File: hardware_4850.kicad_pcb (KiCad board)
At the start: 4 copper layers, 104 x 79 mm, 250 parts, among them J1 +, J10 Enable, J11 CAN_IN, J12 CAN_OUT, J13 Debug, J2 Display, J3 A, J4 HALL, J5 B, J6 MOT_AUX, J7 C, J8 GND, J9 CRANK, P1 SWD, Q1 IPT015N10N5, Q2 IPT015N10N5, Q3 IPT015N10N5, Q4 IPT015N10N5, Q5 IPT015N10N5, Q6 IPT015N10N5, U1 1EDN7550B, U10 LM5008, U11 XC6206P332MR, U12 XC6206P332MR, U13 LMR12010X, U14 STM32G473VCTx, U15 SN65HVD230, U2 INA240A2PWR, U3 1EDN7550B, U4 1EDN7550B, U5 INA240A2PWR, U6 1EDN7550B, U7 1EDN7550B, U8 INA240A2PWR, U9 1EDN7550B, Y1 8MHz

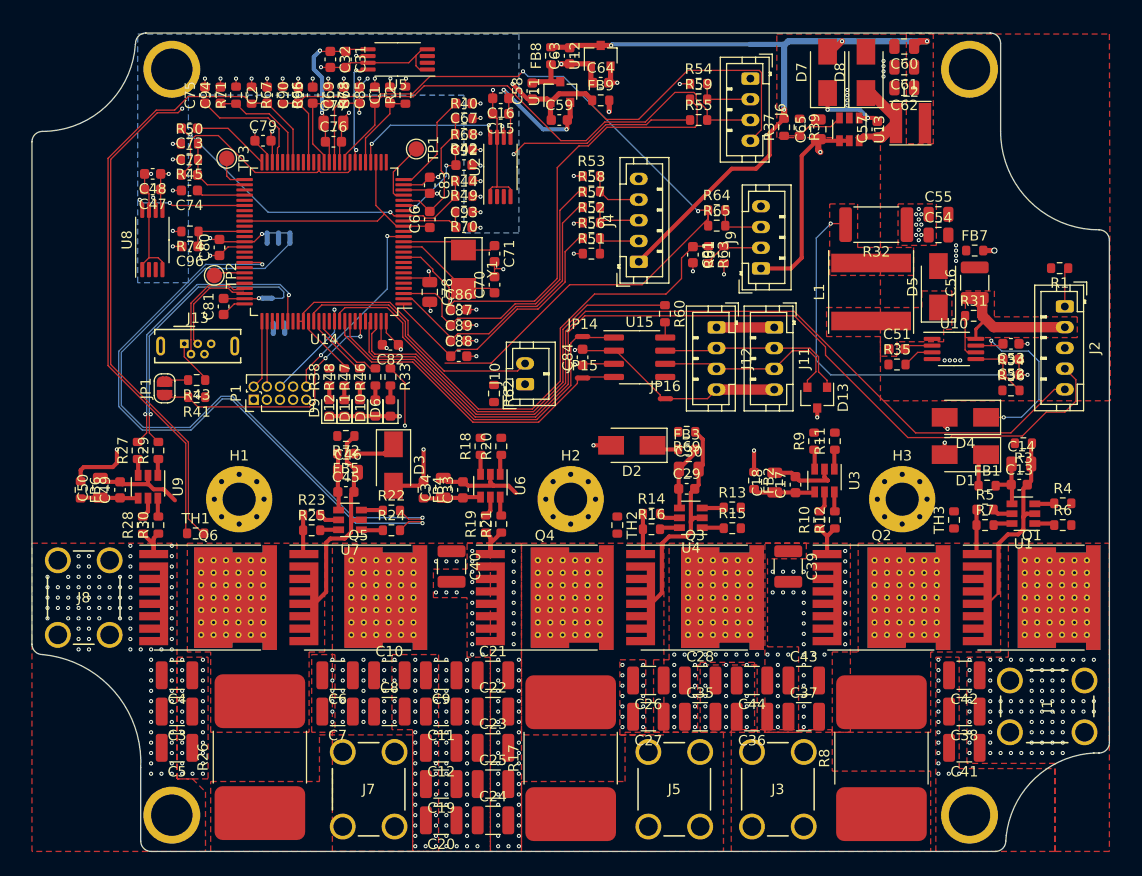
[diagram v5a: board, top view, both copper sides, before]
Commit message: added some more caps for decouppling
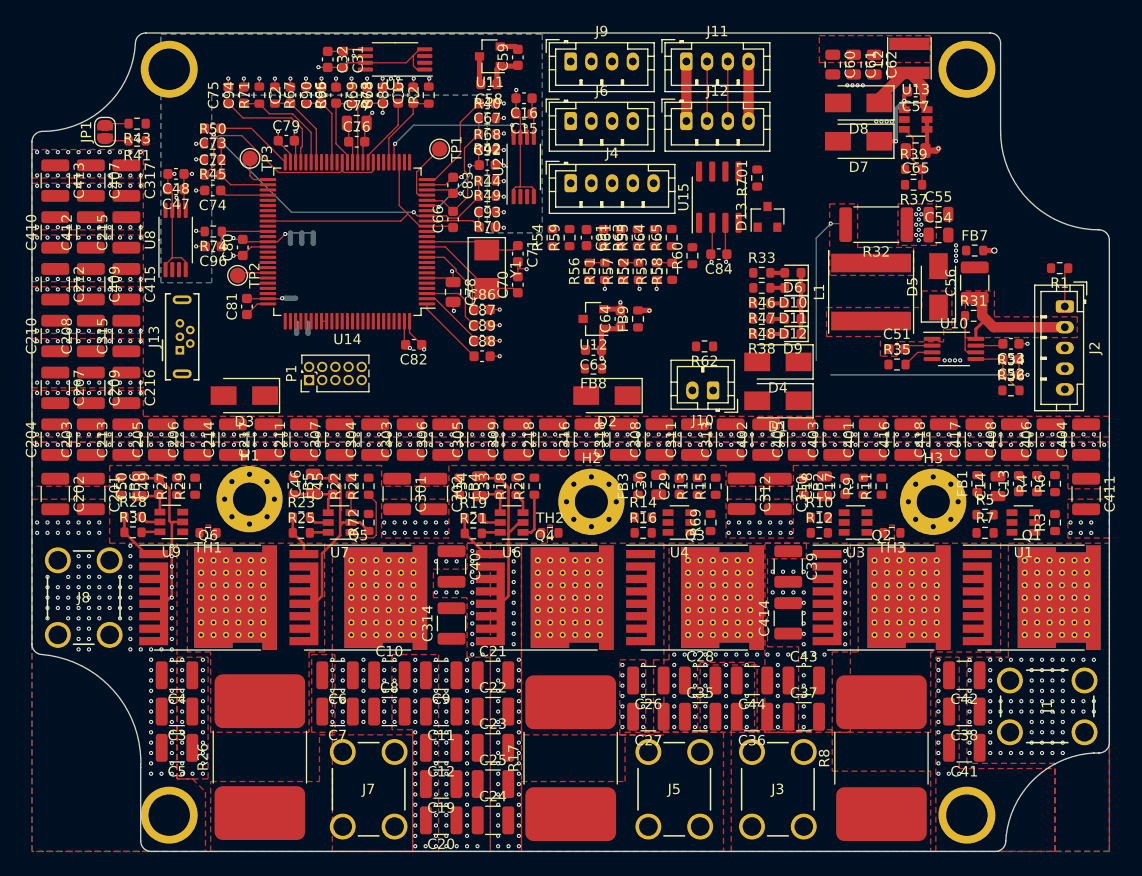
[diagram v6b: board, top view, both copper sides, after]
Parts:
- removed JP14: CAN_TX, NetTie:NetTie-2_SMD_Pad0.5mm
- removed JP15: CAN_RX, NetTie:NetTie-2_SMD_Pad0.5mm
- removed JP16: CAN_GND, NetTie:NetTie-2_SMD_Pad0.5mm
- added C201: 4u7, Capacitor_SMD:C_1210_3225Metric, F.Cu at (83.2, 94.0)
- added C202: 4u7, Capacitor_SMD:C_1210_3225Metric, F.Cu at (79.8, 94.0)
- added C203: 4u7, Capacitor_SMD:C_1210_3225Metric, F.Cu at (83.2, 88.8)
- added C204: 4u7, Capacitor_SMD:C_1210_3225Metric, F.Cu at (79.8, 88.8)
- added C205: 4u7, Capacitor_SMD:C_1210_3225Metric, F.Cu at (90.0, 88.8)
- added C206: 4u7, Capacitor_SMD:C_1210_3225Metric, F.Cu at (93.5, 88.8)
- added C207: 4u7, Capacitor_SMD:C_1210_3225Metric, F.Cu at (79.8, 83.8)
- added C208: 4u7, Capacitor_SMD:C_1210_3225Metric, F.Cu at (83.2, 78.8)
- added C209: 4u7, Capacitor_SMD:C_1210_3225Metric, F.Cu at (83.2, 83.8)
- added C210: 4u7, Capacitor_SMD:C_1210_3225Metric, F.Cu at (79.8, 78.8)
- added C211: 4u7, Capacitor_SMD:C_1210_3225Metric, F.Cu at (103.8, 88.8)
- added C212: 4u7, Capacitor_SMD:C_1210_3225Metric, F.Cu at (79.8, 73.8)
- added C213: 4u7, Capacitor_SMD:C_1210_3225Metric, F.Cu at (86.6, 88.8)
- added C214: 4u7, Capacitor_SMD:C_1210_3225Metric, F.Cu at (96.9, 88.8)
- added C215: 4u7, Capacitor_SMD:C_1210_3225Metric, F.Cu at (86.6, 68.8)
- added C216: 4u7, Capacitor_SMD:C_1210_3225Metric, F.Cu at (86.6, 83.8)
- added C217: 4u7, Capacitor_SMD:C_1210_3225Metric, F.Cu at (100.3, 88.8)
- added C218: 4u7, Capacitor_SMD:C_1210_3225Metric, F.Cu at (127.8, 88.8)
- added C301: 4u7, Capacitor_SMD:C_1210_3225Metric, F.Cu at (112.8, 94.0)
- added C302: 4u7, Capacitor_SMD:C_1210_3225Metric, F.Cu at (116.2, 94.0)
- added C303: 4u7, Capacitor_SMD:C_1210_3225Metric, F.Cu at (114.1, 88.8)
- added C304: 4u7, Capacitor_SMD:C_1210_3225Metric, F.Cu at (110.6, 88.8)
- added C305: 4u7, Capacitor_SMD:C_1210_3225Metric, F.Cu at (120.9, 88.8)
- added C306: 4u7, Capacitor_SMD:C_1210_3225Metric, F.Cu at (117.5, 88.8)
- added C307: 4u7, Capacitor_SMD:C_1210_3225Metric, F.Cu at (107.2, 88.8)
- added C308: 4u7, Capacitor_SMD:C_1210_3225Metric, F.Cu at (138.1, 88.8)
- added C309: 4u7, Capacitor_SMD:C_1210_3225Metric, F.Cu at (124.4, 88.8)
- added C310: 4u7, Capacitor_SMD:C_1210_3225Metric, F.Cu at (149.5, 94.0)
- added C311: 4u7, Capacitor_SMD:C_1210_3225Metric, F.Cu at (141.5, 88.8)
- added C312: 4u7, Capacitor_SMD:C_1210_3225Metric, F.Cu at (146.0, 94.0)
- added C313: 4u7, Capacitor_SMD:C_1210_3225Metric, F.Cu at (144.9, 88.8)
- added C314: 4u7, Capacitor_SMD:C_1210_3225Metric, F.Cu at (118.0, 106.5)
- added C315: 4u7, Capacitor_SMD:C_1210_3225Metric, F.Cu at (86.6, 78.8)
- added C316: 4u7, Capacitor_SMD:C_1210_3225Metric, F.Cu at (131.2, 88.8)
- added C317: 4u7, Capacitor_SMD:C_1210_3225Metric, F.Cu at (86.6, 63.8)
- added C318: 4u7, Capacitor_SMD:C_1210_3225Metric, F.Cu at (134.6, 88.8)
- added C401: 4u7, Capacitor_SMD:C_1210_3225Metric, F.Cu at (158.7, 88.8)
- added C402: 4u7, Capacitor_SMD:C_1210_3225Metric, F.Cu at (148.4, 88.8)
- added C403: 4u7, Capacitor_SMD:C_1210_3225Metric, F.Cu at (155.2, 88.8)
- added C404: 4u7, Capacitor_SMD:C_1210_3225Metric, F.Cu at (179.2, 88.8)
- added C405: 4u7, Capacitor_SMD:C_1210_3225Metric, F.Cu at (151.8, 88.8)
- added C406: 4u7, Capacitor_SMD:C_1210_3225Metric, F.Cu at (175.8, 88.8)
- added C407: 4u7, Capacitor_SMD:C_1210_3225Metric, F.Cu at (83.2, 63.8)
- added C408: 4u7, Capacitor_SMD:C_1210_3225Metric, F.Cu at (172.4, 88.8)
- added C409: 4u7, Capacitor_SMD:C_1210_3225Metric, F.Cu at (83.2, 73.8)
- added C410: 4u7, Capacitor_SMD:C_1210_3225Metric, F.Cu at (79.8, 68.8)
- added C411: 4u7, Capacitor_SMD:C_1210_3225Metric, F.Cu at (179.2, 94.0)
- added C412: 4u7, Capacitor_SMD:C_1210_3225Metric, F.Cu at (83.2, 68.8)
- added C413: 4u7, Capacitor_SMD:C_1210_3225Metric, F.Cu at (79.8, 63.8)
- added C414: 4u7, Capacitor_SMD:C_1210_3225Metric, F.Cu at (150.5, 106.0)
- added C415: 4u7, Capacitor_SMD:C_1210_3225Metric, F.Cu at (86.6, 73.8)
- added C416: 4u7, Capacitor_SMD:C_1210_3225Metric, F.Cu at (162.1, 88.8)
- added C417: 4u7, Capacitor_SMD:C_1210_3225Metric, F.Cu at (169.0, 88.8)
- added C418: 4u7, Capacitor_SMD:C_1210_3225Metric, F.Cu at (165.5, 88.8)
- added R701: 1R, Resistor_SMD:R_0603_1608Metric, F.Cu at (147.5, 63.5)
- moved D9 45.3 mm to (150.9, 78.5), turned to 180 degrees
- moved D12 44.1 mm to (150.9, 77.1), turned to 180 degrees
- moved D11 43.0 mm to (150.9, 75.6), turned to 180 degrees
- moved R38 42.0 mm to (147.9, 78.5), turned to 180 degrees
- moved D10 41.9 mm to (150.9, 74.1), turned to 180 degrees
- moved D6 41.0 mm to (150.9, 72.7), turned to 180 degrees
- moved R48 40.7 mm to (147.9, 77.1), turned to 180 degrees
- moved R47 39.4 mm to (147.9, 75.6), turned to 180 degrees
- moved R46 38.3 mm to (147.9, 74.1), turned to 180 degrees
- moved R33 37.2 mm to (147.9, 72.7), turned to 0 degrees
- moved FB8 30.5 mm to (131.7, 81.9), turned to 180 degrees
- moved C63 28.5 mm to (131.7, 80.1), turned to 180 degrees
- moved J9 27.1 mm to (129.5, 52.2), turned to 0 degrees
- moved J11 27.0 mm to (140.7, 52.2), turned to 0 degrees
- moved U12 25.4 mm to (131.7, 77.1), turned to 180 degrees
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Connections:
- U15 pad 1: Net-(JP14-Pad2) -> /Interface/CAN_TX
- U15 pad 4: Net-(JP15-Pad2) -> /Interface/CAN_RX
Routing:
- net GNDPWR: track 158.7 -> 39.0 mm, vias 296 -> 502
- net /mcu/DISP_TX: track 91.2 -> 0.00 mm
- net /mcu/DISP_RX: track 86.1 -> 0.00 mm
- net GNDA: track 151.7 -> 69.2 mm, vias 28 -> 26
- net /mcu/AIN_CRK_TORQ: track 87.6 -> 7.63 mm, vias 2 -> 0
- net +5V: track 68.0 -> 0.00 mm, vias 4 -> 0
- net /mcu/PWM_C-: track 64.4 -> 0.00 mm, vias 1 -> 0
- net /mcu/PWM_C+: track 63.5 -> 0.00 mm, vias 2 -> 0
- net /mcu/AIN_TEMP_A: track 64.2 -> 8.26 mm
- net /Interface/PULSE_CRK: track 54.9 -> 0.00 mm
- net /Interface/CAN_SLP: track 44.6 -> 0.00 mm
- net /mcu/AIN_TEMP_MOT: track 50.0 -> 6.90 mm
- net +12V: track 45.4 -> 4.39 mm, vias 18 -> 11
- net /Interface/PULSE_MOT: track 48.4 -> 7.90 mm
- net /Interface/CAN_TX: track 32.5 -> 0.00 mm
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- added copper zone on B.Cu, net +BATT
- removed copper zone on VCC, net +12V
- removed copper zone on F.Cu, net GNDD
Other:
- outline, holes or cut-outs redrawn
